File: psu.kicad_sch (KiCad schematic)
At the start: 76 parts, among them J1 39-28-1243, J2 292161-3, J3 292161-3, J4 292161-3, J5 292161-3, J6 292161-3, Q1 IRLML6344TRPBF, Q2 BSS138, Q3 IRLML6344TRPBF, Q4 IRLML6344TRPBF, U1 AZ1117-3.3

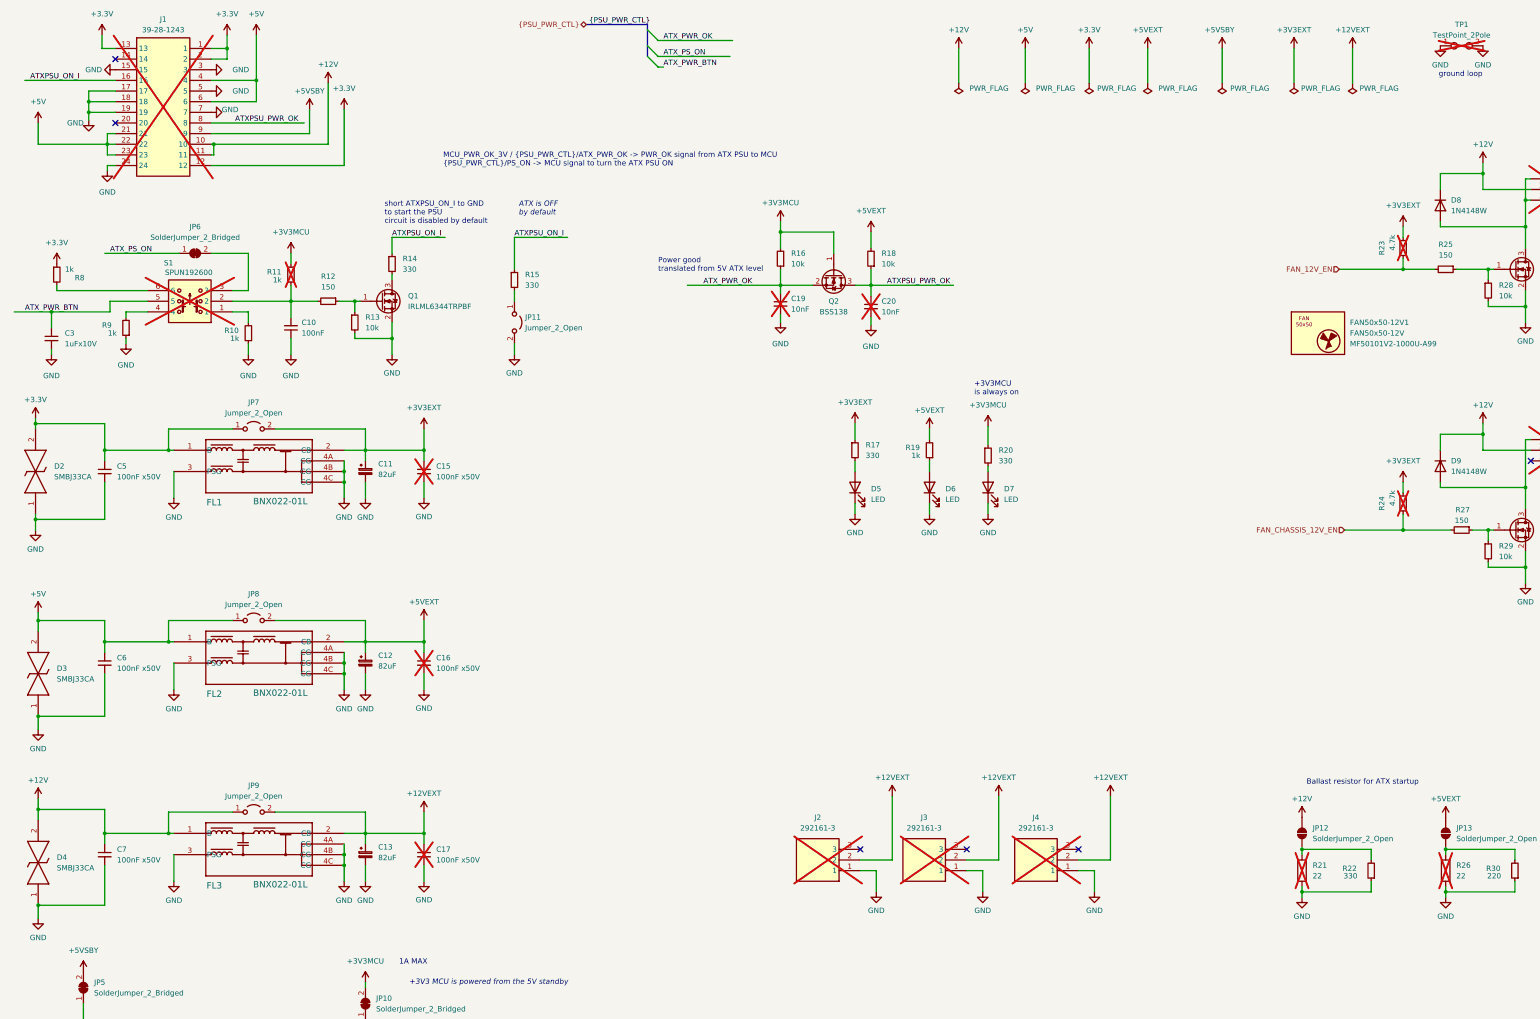
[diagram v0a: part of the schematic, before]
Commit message: PW filters, power GND goes to pin 3
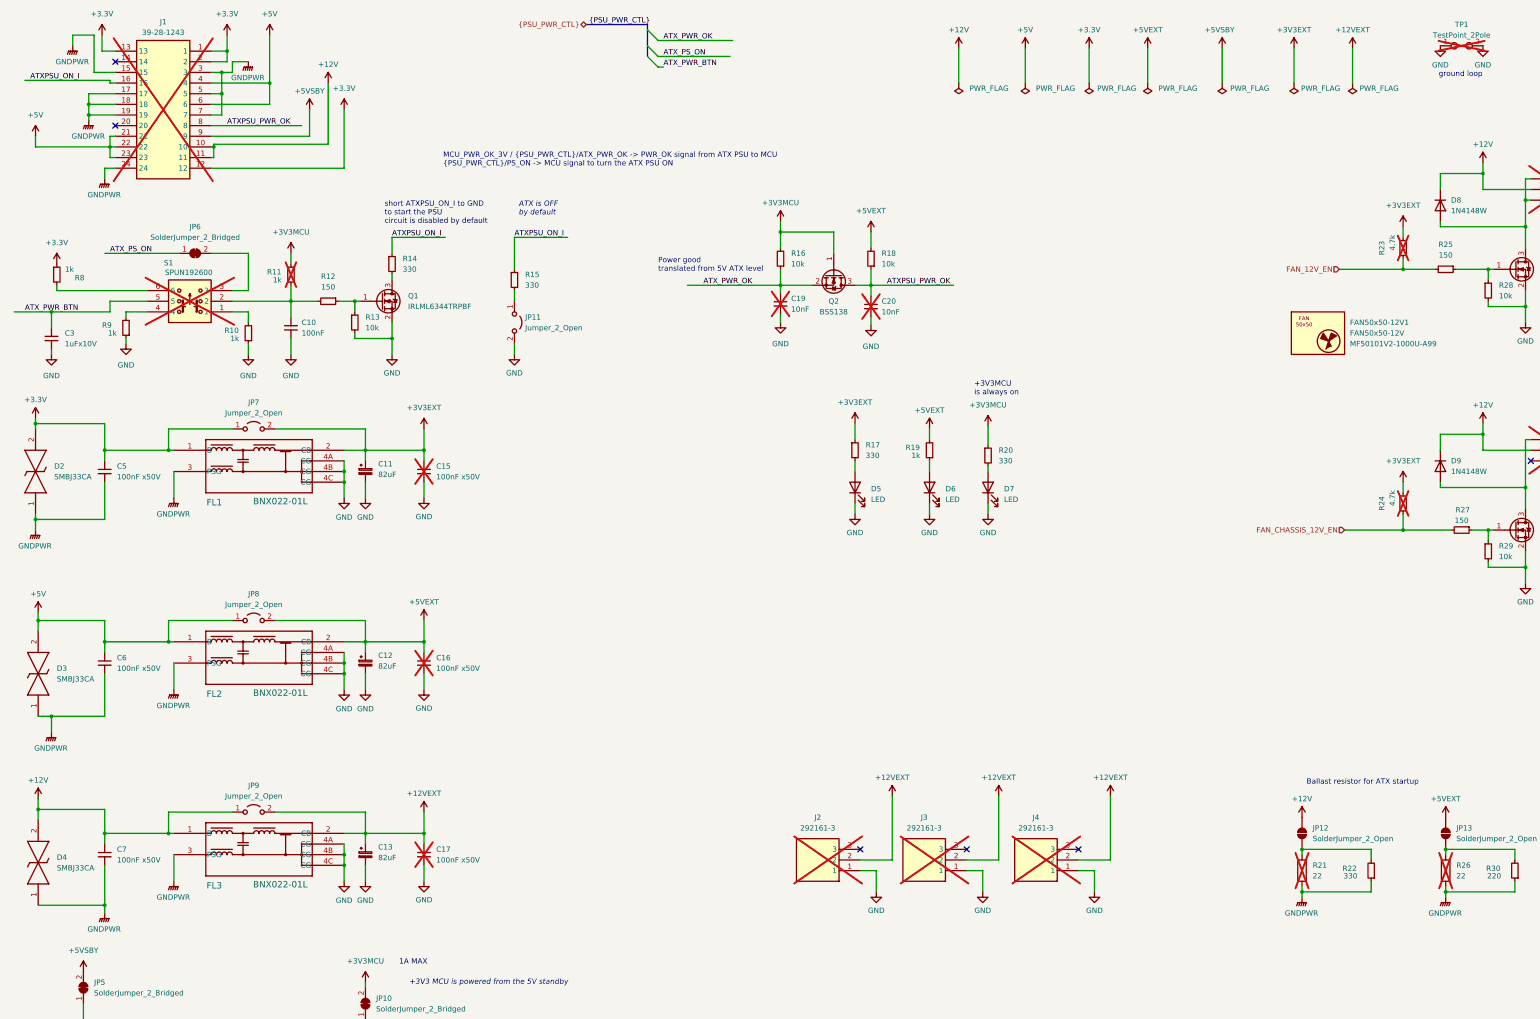
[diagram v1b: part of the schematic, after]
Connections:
- net GND: no longer C5.2, C6.2, C7.2, D2.1, D3.1, D4.1, FL1.3 (PSG), FL2.3 (PSG), FL3.3 (PSG), J1.15, J1.17, J1.18, J1.19, J1.24, J1.3, J1.5, J1.7, R21.2, R22.1, R26.2, R30.1
- new net GNDPWR: C5.2, C6.2, C7.2, D2.1, D3.1, D4.1, FL1.3 (PSG), FL2.3 (PSG), FL3.3 (PSG), J1.15, J1.17, J1.18, J1.19, J1.24, J1.3, J1.5, J1.7, R21.2, R22.1, R26.2, R30.1
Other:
- moved on the sheet: J1
